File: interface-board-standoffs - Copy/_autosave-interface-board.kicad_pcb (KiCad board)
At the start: 2 copper layers, 181.5 x 110 mm, 83 parts, among them J1 HECS, J11 UART, J12 NTC1, J13 NTC1, J15 ICSP, J16 AMPSEAL, J2 CASEFAN1, J3 CASEFAN2, J4 Bender-LV, J5 BLINKY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

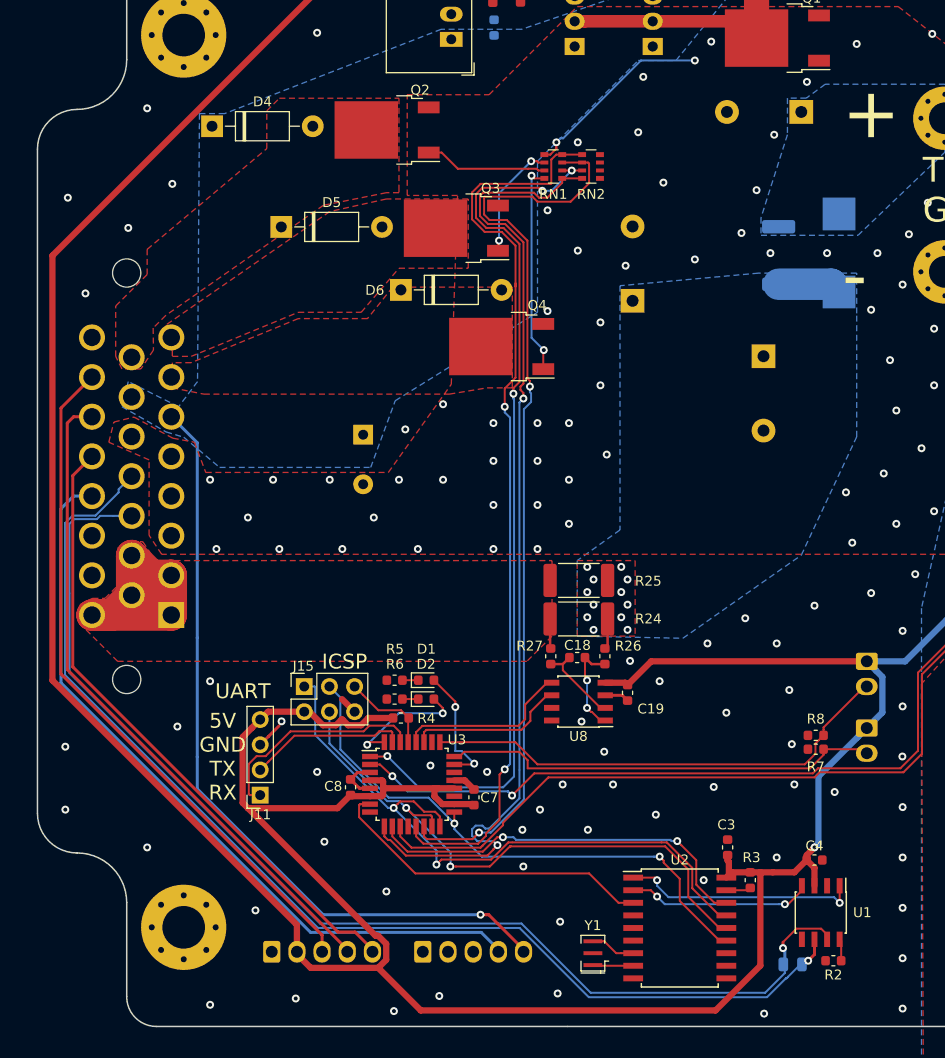
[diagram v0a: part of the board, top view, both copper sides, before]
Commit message: Made lots of gerbers, shipped boards.
Also, re-routed interface-board to be 8/8mil minimum spacing.
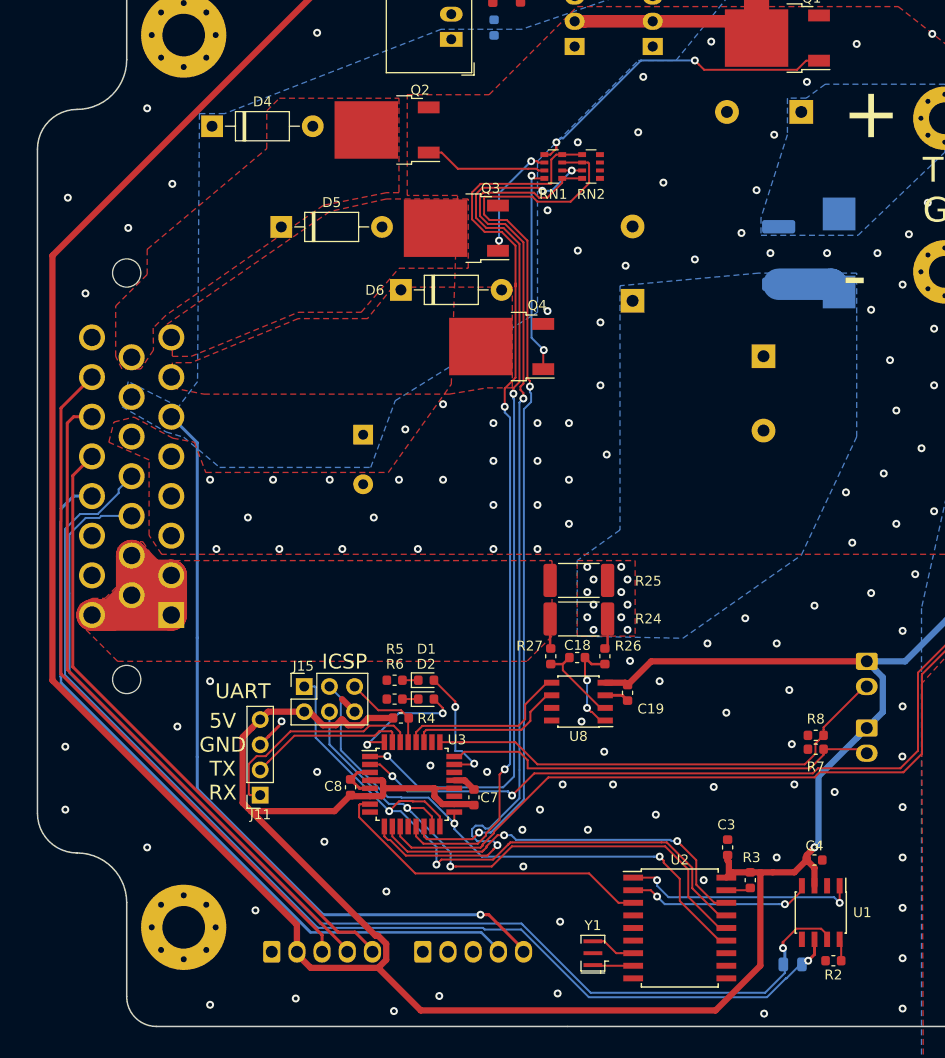
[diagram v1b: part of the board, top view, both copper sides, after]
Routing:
- net Net-(Q1-Pad1): track 19.5 -> 32.8 mm
- net /Main/sheet5C830476/MISO: track 65.4 -> 67.6 mm
- net /Main/sheet5C830476/MOSI: track 58.8 -> 59.8 mm
- net /Main/CAN+: track 116.9 -> 116.3 mm
- net Net-(Q4-Pad1): track 22.0 -> 21.4 mm
